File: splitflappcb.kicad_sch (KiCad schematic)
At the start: 43 parts, among them J1 Conn_01x04_Pin, J2 Conn_01x04_Pin, J3 Conn_01x05_Pin, J4 AddressJumpers, J5 HallSensor, J6 AVR-ISP-6, J7 Serial-328P, J8 Serial-ESP12E, J9 WS2815, SW1 RESET, U2 ULN2003A, U3 ATmega328P-A, U3 TPS5430, U4 ESP-12E, Y2 16MHz

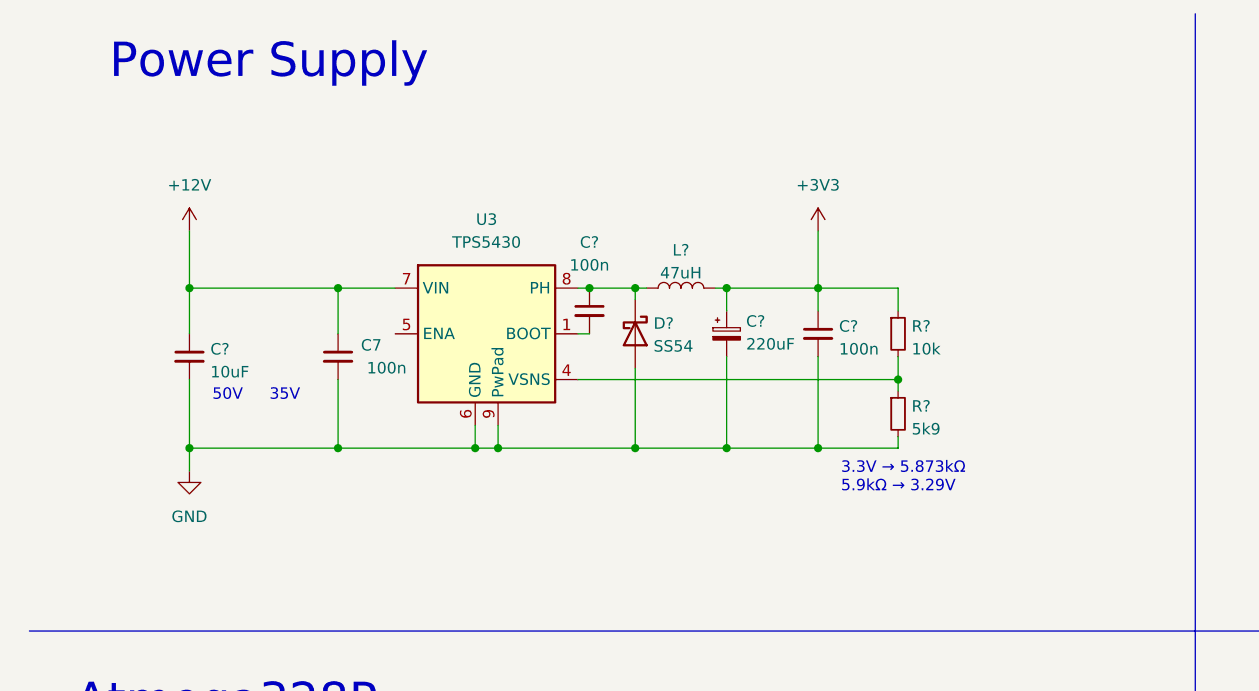
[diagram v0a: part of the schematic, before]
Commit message: Changed out a tantalum capacitor for four better ones
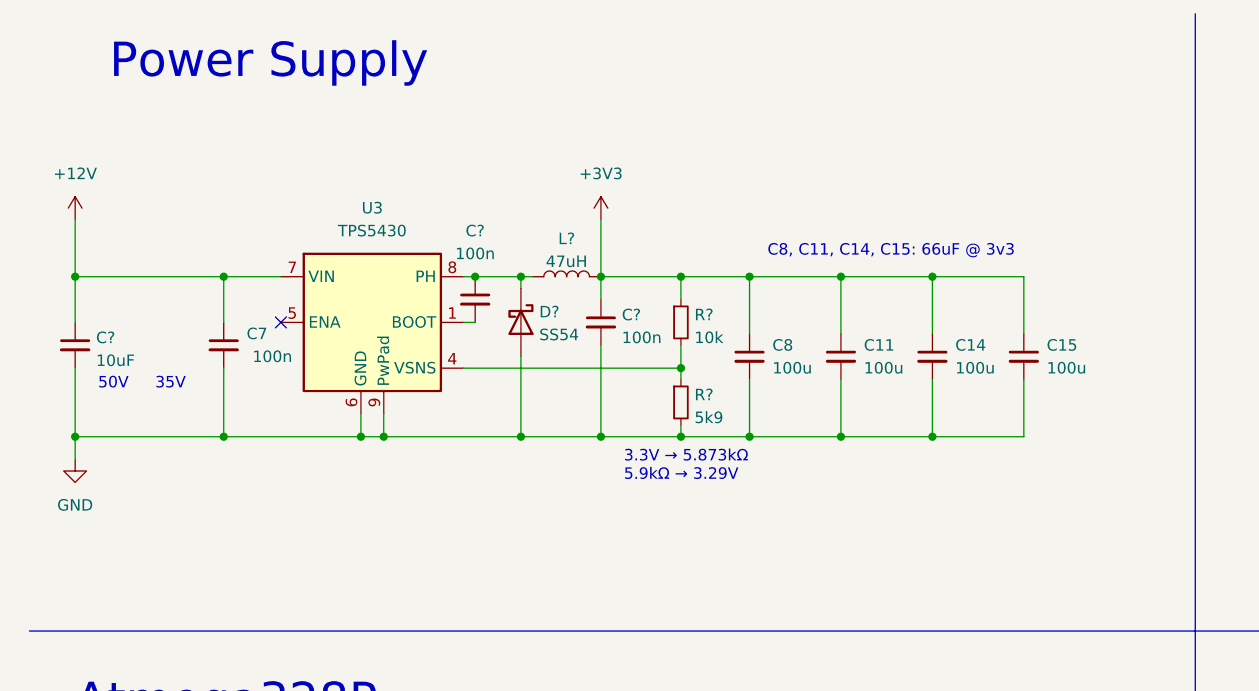
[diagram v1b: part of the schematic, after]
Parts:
- removed C?: 220uF, Capacitor_Tantalum_SMD:CP_EIA-3528-21_Kemet-B, symbol Device:C_Polarized_Small
- added C11, C14, C15, C8: 100u, Capacitor_SMD:C_1206_3216Metric, symbol Device:C_Small
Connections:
- net +3V3: now also C11.1, C14.1, C15.1, C8.1
- net GND: now also C11.2, C14.2, C15.2, C8.2
- no-connect marks 0 -> 1
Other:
- note added: "C8, C11, C14, C15: 66uF @ 3v3"
- moved on the sheet: C7, C?, D?, L?, R?, U3

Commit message: ordered rev1
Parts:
- removed C1, C2: 22pF, Capacitor_SMD:C_0402_1005Metric, symbol Device:C_Small
- removed C11, C14, C15: 100u, Capacitor_SMD:C_1206_3216Metric, symbol Device:C_Small
- removed C13, C4, C6, C? (x2): 100n, Capacitor_SMD:C_0402_1005Metric, symbol Device:C_Small
- removed C3, C5, C?: 10uF, Capacitor_SMD:C_0805_2012Metric, symbol Device:C_Small
- removed D1: LED, LED_SMD:LED_0805_2012Metric, symbol Device:LED
- removed D? (x2): SS54, Diode_SMD:D_SMA, symbol Device:D_Schottky
- removed H1, H2, H3, H4: MountingHole_Pad, MountingHole:MountingHole_3.2mm_M3_DIN965_Pad, symbol Mechanical:MountingHole_Pad
- removed J1, J2: Conn_01x04_Pin, Connector_JST:JST_XH_B4B-XH-AM_1x04_P2.50mm_Vertical, symbol Connector:Conn_01x04_Pin
- removed J3: Conn_01x05_Pin, Connector_JST:JST_XH_B5B-XH-AM_1x05_P2.50mm_Vertical, symbol Connector:Conn_01x05_Pin
- removed J4: AddressJumpers, Connector_PinHeader_2.54mm:PinHeader_2x08_P2.54mm_Vertical, symbol Connector_Generic:Conn_02x08_Odd_Even
- removed J5: HallSensor, Connector_JST:JST_XH_B3B-XH-AM_1x03_P2.50mm_Vertical, symbol Connector:Conn_01x03_Pin
- removed J6: AVR-ISP-6, Connector_PinHeader_2.54mm:PinHeader_2x03_P2.54mm_Vertical, symbol Connector:AVR-ISP-6
- removed J7: Serial-328P, Connector_PinHeader_2.54mm:PinHeader_1x05_P2.54mm_Vertical, symbol Connector:Conn_01x05_Pin
- removed J8: Serial-ESP12E, Connector_PinHeader_2.54mm:PinHeader_1x06_P2.54mm_Vertical, symbol Connector:Conn_01x06_Pin
- removed J9: WS2815, Connector_JST:JST_XH_B3B-XH-AM_1x03_P2.50mm_Vertical, symbol Connector:Conn_01x03_Pin
- removed L?: 47uH, Inductor_SMD:L_Chilisin_BMRx00060630, symbol Device:L
- removed R1: 220, Resistor_SMD:R_0402_1005Metric, symbol Device:R_Small
- removed R2, R5, R6, R7, R8, R?: 10k, Resistor_SMD:R_0402_1005Metric, symbol Device:R_Small
- removed R?: 5k9, Resistor_SMD:R_0402_1005Metric, symbol Device:R_Small
- removed SW1: RESET, Button_Switch_SMD:SW_SPST_SKQG_WithStem, symbol Switch:SW_Push
- removed U2: ULN2003A, Package_SO:SOIC-16_3.9x9.9mm_P1.27mm, symbol Transistor_Array:ULN2003A
- removed U3: TPS5430, Package_SO:SOIC-8-1EP_3.9x4.9mm_P1.27mm_EP2.514x3.2mm_ThermalVias, symbol opendcc:TPS5450
- removed U3: ATmega328P-A, Package_QFP:TQFP-32_7x7mm_P0.8mm, symbol MCU_Microchip_ATmega:ATmega328P-A
- removed U4: ESP-12E, RF_Module:ESP-12E, symbol RF_Module:ESP-12E
- removed Y2: 16MHz, Crystal:Crystal_SMD_3225-4Pin_3.2x2.5mm, symbol Device:Crystal_GND24_Small
- added C10, C12, C9: 10u, Capacitor_SMD:C_0603_1608Metric, symbol Device:C_Small
- added J1, J17: Conn_01x04_Pin, Connector_JST:JST_XH_B6B-XH-AM_1x06_P2.50mm_Vertical, symbol Connector:Conn_01x06_Pin
- added J12: Conn_ARM_SWD_TagConnect_TC2030-NL, Connector:Tag-Connect_TC2030-IDC-NL_2x03_P1.27mm_Vertical, symbol Connector:Conn_ARM_SWD_TagConnect_TC2030-NL
- added J15: Conn_01x03_Pin, Connector_PinHeader_2.54mm:PinHeader_1x03_P2.54mm_Vertical, symbol Connector:Conn_01x03_Pin
- added J9: Conn_01x04_Pin, Connector_PinHeader_2.54mm:PinHeader_1x04_P2.54mm_Vertical, symbol Connector:Conn_01x04_Pin
- added JP1: Jumper_2_Small_Bridged, Jumper:SolderJumper-2_P1.3mm_Bridged_RoundedPad1.0x1.5mm, symbol Jumper:Jumper_2_Small_Bridged
- added JP2: Jumper_2_Small_Open, Jumper:SolderJumper-2_P1.3mm_Open_RoundedPad1.0x1.5mm, symbol Jumper:Jumper_2_Small_Open
- added U4: STM32F030C8Tx, Package_QFP:LQFP-48_7x7mm_P0.5mm, symbol MCU_ST_STM32F0:STM32F030C8Tx
- C7: footprint Capacitor_SMD:C_0402_1005Metric -> Capacitor_SMD:C_0603_1608Metric; LCSC C307331 -> C14663
- C8: value 100u -> 10u; footprint Capacitor_SMD:C_1206_3216Metric -> Capacitor_SMD:C_0603_1608Metric; LCSC (none) -> C19702
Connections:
- net +12V: now also J1.5 (Pin_5), J1.6 (Pin_6), J15.1 (Pin_1), J17.5 (Pin_5), J17.6 (Pin_6); no longer C7.1
- net +3V3: now also C10.1, C12.1, C9.1, J1.4 (Pin_4), J12.1 (VCC), J15.3 (Pin_3), J17.4 (Pin_4), J9.4 (Pin_4), JP2.2 (B), U4.1 (VDD), U4.24 (VDD), U4.48 (VDD), U4.9 (VDDA)
- net GND: now also C10.2, C12.2, C9.2, J1.1 (Pin_1), J1.2 (Pin_2), J12.5 (GND), J15.2 (Pin_2), J17.1 (Pin_1), J17.2 (Pin_2), J9.1 (Pin_1), JP1.2 (B), U4.23 (VSS), U4.47 (VSS), U4.8 (VSSA)
- new net 1_1: U4.28 (PB15)
- new net 1_2: U4.27 (PB14)
- new net 1_3: U4.26 (PB13)
- new net 1_4: U4.25 (PB12)
- new net 1_H: U4.29 (PA8)
- new net 2_1: U4.18 (PB0)
- new net 2_2: U4.17 (PA7)
- new net 2_3: U4.16 (PA6)
- new net 2_4: U4.15 (PA5)
- new net 2_H: U4.19 (PB1)
- new net 3_1: U4.13 (PA3)
- new net 3_2: U4.12 (PA2)
- new net 3_3: U4.11 (PA1)
- new net 3_4: U4.10 (PA0)
- new net 3_H: U4.14 (PA4)
- new net 4_1: U4.5 (PF0)
- new net 4_2: U4.4 (PC15)
- new net 4_3: U4.3 (PC14)
- new net 4_4: U4.2 (PC13)
- new net 4_H: U4.6 (PF1)
- new net 5_1: U4.42 (PB6)
- new net 5_2: U4.41 (PB5)
- new net 5_3: U4.40 (PB4)
- new net 5_4: U4.39 (PB3)
- new net 5_H: U4.43 (PB7)
- new net 6_1: U4.36 (PF7)
- new net 6_2: U4.35 (PF6)
- new net 6_3: U4.33 (PA12)
- new net 6_4: U4.32 (PA11)
- new net 6_H: U4.38 (PA15)
- new net BOOT0: JP1.1 (A), U4.44 (BOOT0)
- new net DATA_IN: J17.3 (Pin_3), U4.31 (PA10)
- new net DATA_OUT: J1.3 (Pin_3), U4.30 (PA9)
- new net NRST: C7.1, JP2.1 (A), U4.7 (NRST)
- new net SWCLK: J12.4 (SWCLK), J9.3 (Pin_3), U4.37 (PA14)
- new net SWDIO: J12.2 (SWDIO), J9.2 (Pin_2), U4.34 (PA13)
- no-connect marks 1 -> 6
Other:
- added sheet stepper1 (driver.kicad_sch)
- added sheet stepper2 (driver.kicad_sch)
- added sheet stepper3 (driver.kicad_sch)
- added sheet stepper4 (driver.kicad_sch)
- added sheet stepper5 (driver.kicad_sch)
- added sheet stepper6 (driver.kicad_sch)
- note added: "STM32"
- note removed: "3.3V → 5.873kΩ 5.9kΩ → 3.29V"
- note removed: "35V"
- note removed: "50V"
- note removed: "Atmega328P"
- note removed: "C8, C11, C14, C15: 66uF @ 3v3"
- note removed: "Connectors"
- note removed: "ESP8266"
- note removed: "Power Supply"
